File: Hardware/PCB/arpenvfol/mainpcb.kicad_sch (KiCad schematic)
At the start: 58 parts, among them J2 AudioJack2, J3 AudioJack2_SwitchT, J4 AudioJack2_SwitchT, J5 AudioJack2, J6 AudioJack2, Q1 2N3904, Q2 2N3904, U1 TL074

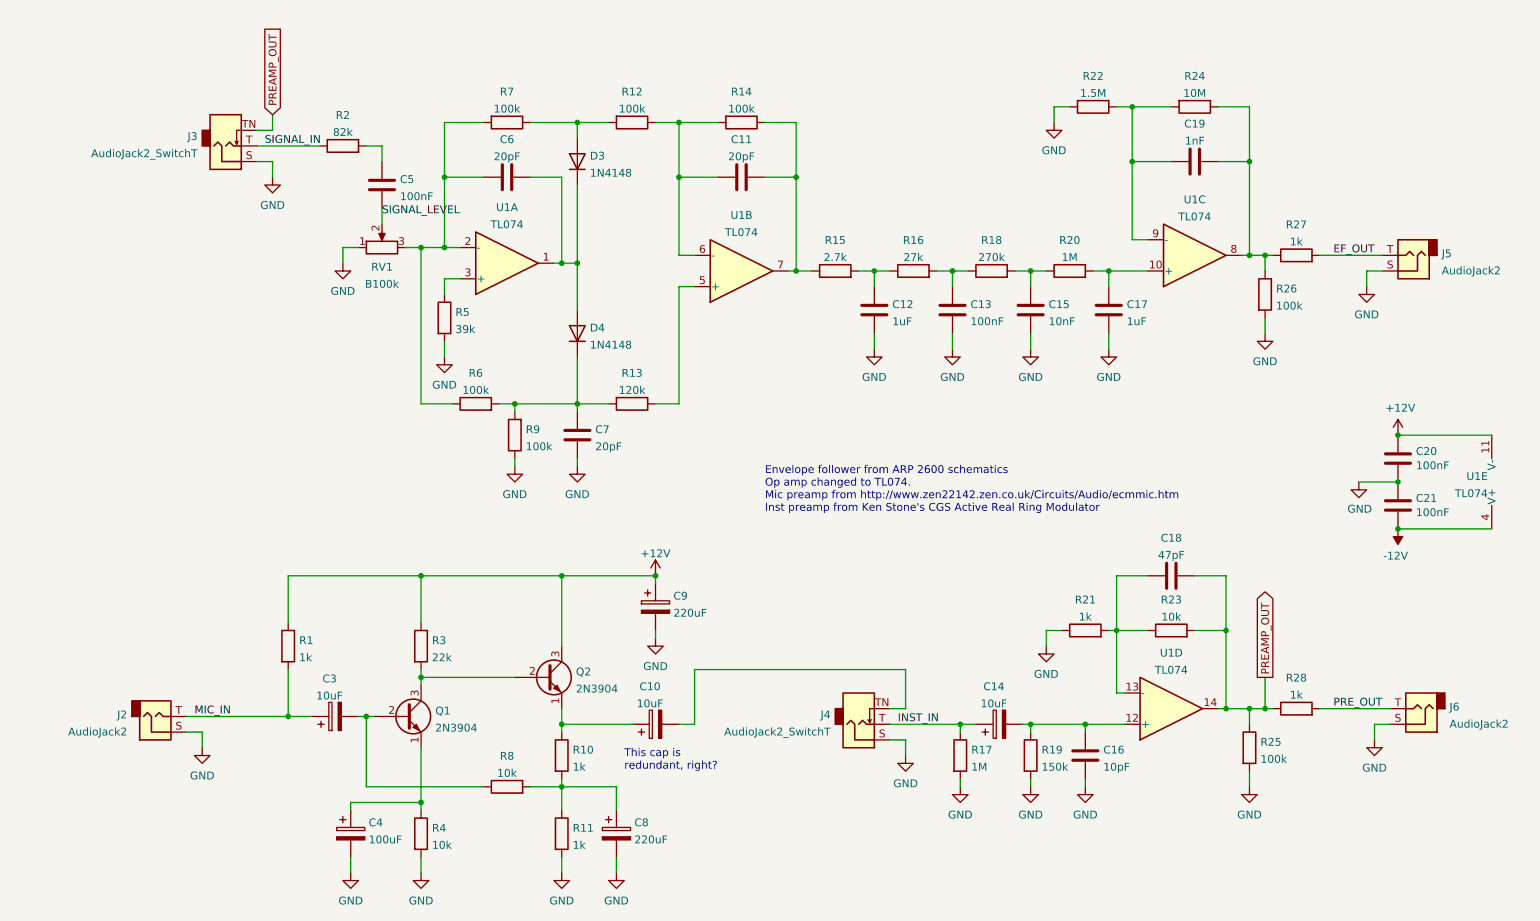
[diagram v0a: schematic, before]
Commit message: rm cap, add mic
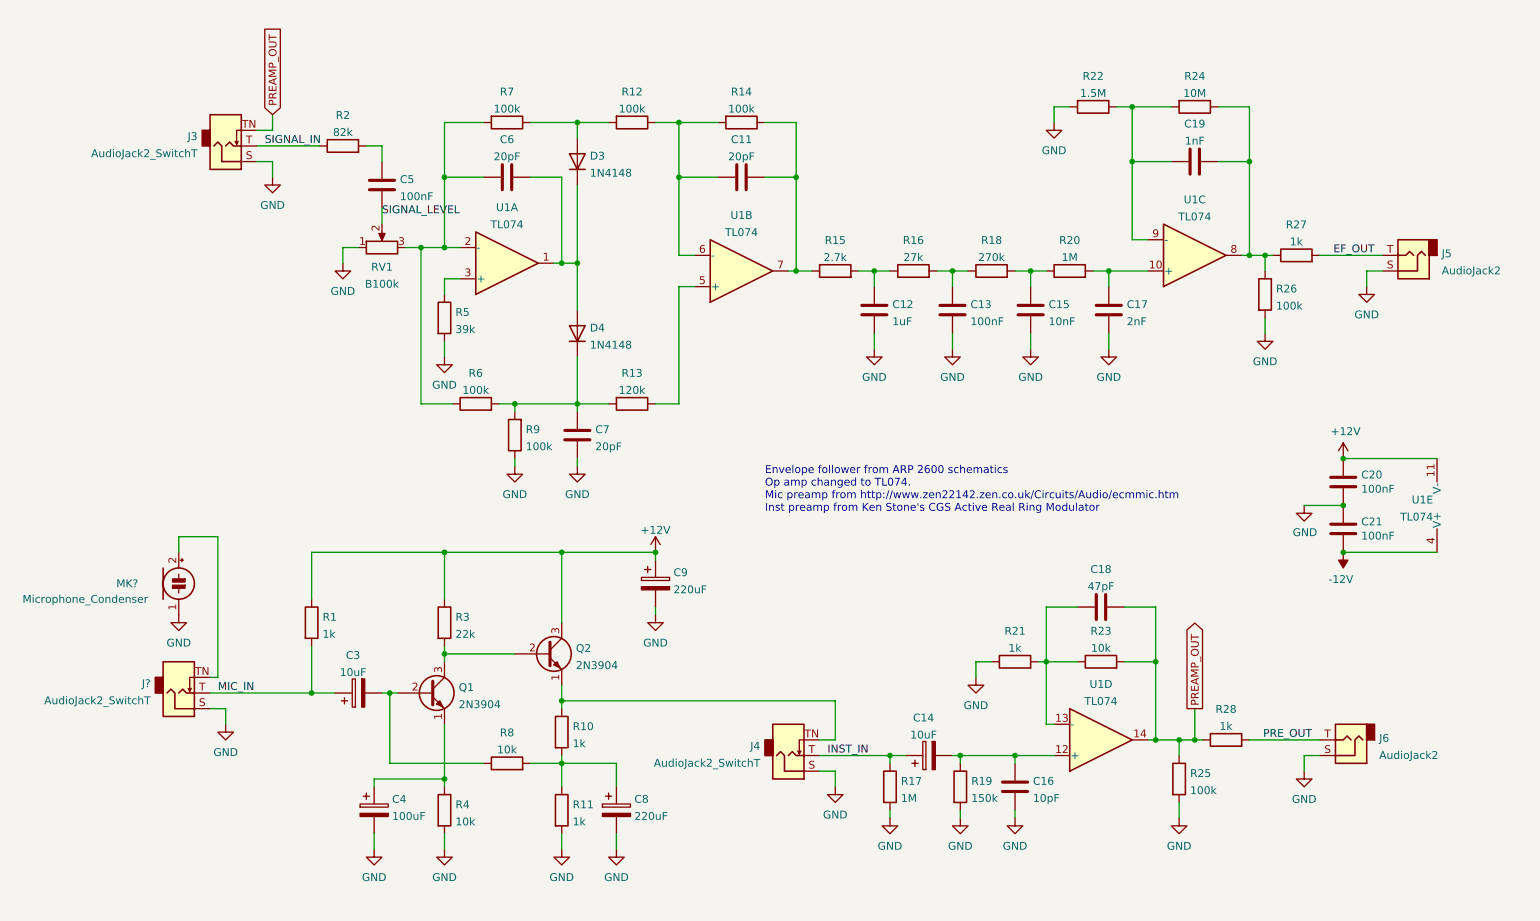
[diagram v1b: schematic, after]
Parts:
- removed C10: 10uF, ao_tht:CP_Radial_D6.3mm_P2.50mm, symbol ao_symbols:CP
- removed J2: AudioJack2, symbol Connector:AudioJack2
- added J?: AudioJack2_SwitchT, symbol Connector:AudioJack2_SwitchT
- added MK?: Microphone_Condenser, symbol Device:Microphone_Condenser
- C17: value 1uF -> 2nF
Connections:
- net GND: now also J?.S, MK?.1 (-)
- net MIC_IN: now also J?.T
- net at Q2.1 (E), R10.1: now also J4.TN
- new net: J?.TN, MK?.2 (+)
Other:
- note removed: "This cap is redundant, right?"
- moved on the sheet: C14, C16, C18, C20, C21, C3, C4, C8, C9, J4, J6, Q1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
